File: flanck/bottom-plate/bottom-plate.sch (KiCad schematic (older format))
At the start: 55 parts, among them SW1 SW_PUSH, SW10 SW_PUSH, SW11 SW_PUSH, SW12 SW_PUSH, SW13 SW_PUSH, SW14 SW_PUSH, SW15 SW_PUSH, SW16 SW_PUSH, SW17 SW_PUSH, SW18 SW_PUSH, SW19 SW_PUSH, SW2 SW_PUSH, SW20 SW_PUSH, SW21 SW_PUSH, SW22 SW_PUSH, SW23 SW_PUSH, SW24 SW_PUSH, SW25 SW_PUSH, SW26 SW_PUSH, SW27 SW_PUSH, SW28 SW_PUSH, SW29 SW_PUSH, SW3 SW_PUSH, SW30 SW_PUSH, SW31 SW_PUSH, SW32 SW_PUSH, SW33 SW_PUSH, SW34 SW_PUSH, SW35 SW_PUSH, SW36 SW_PUSH, SW37 SW_PUSH, SW38 SW_PUSH, SW39 SW_PUSH, SW4 SW_PUSH, SW40 SW_PUSH, SW41 SW_PUSH, SW42 SW_PUSH, SW43 SW_PUSH, SW44 SW_PUSH, SW45 SW_PUSH, SW46 SW_PUSH, SW47 SW_PUSH, SW48 SW_PUSH, SW5 SW_PUSH, SW6 SW_PUSH, SW7 SW_PUSH, SW8 SW_PUSH, SW9 SW_PUSH

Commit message: bottom plate
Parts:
- removed SW1, SW10, SW11, SW12, SW13, SW14, SW15, SW16, SW17, SW18, SW19, SW2, SW20, SW21, SW22, SW23, SW24, SW25, SW26, SW27, SW28, SW29, SW3, SW30, SW31, SW32, SW33, SW34, SW35, SW36, SW37, SW38, SW39, SW4, SW40, SW41, SW42, SW43, SW44, SW45, SW46, SW47, SW48, SW5, SW6, SW7, SW8, SW9: SW_PUSH, kbd:SW_Hole, symbol kbd:SW_PUSH

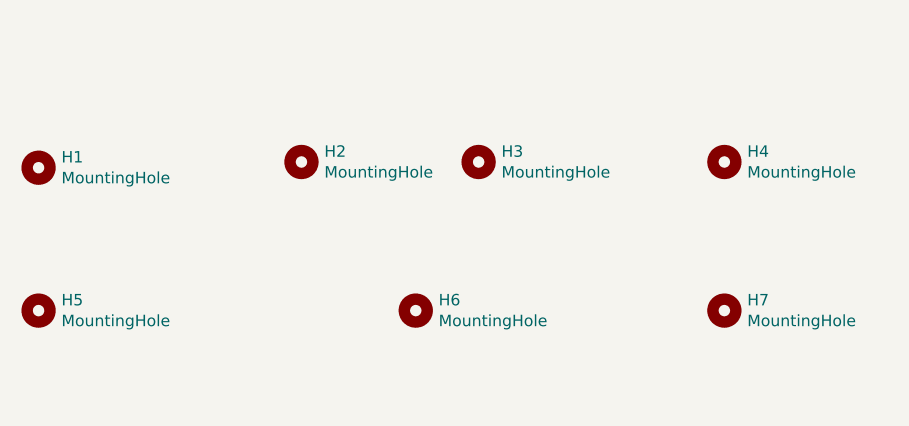
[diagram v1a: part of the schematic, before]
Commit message: fix pcb mounting hole sizes
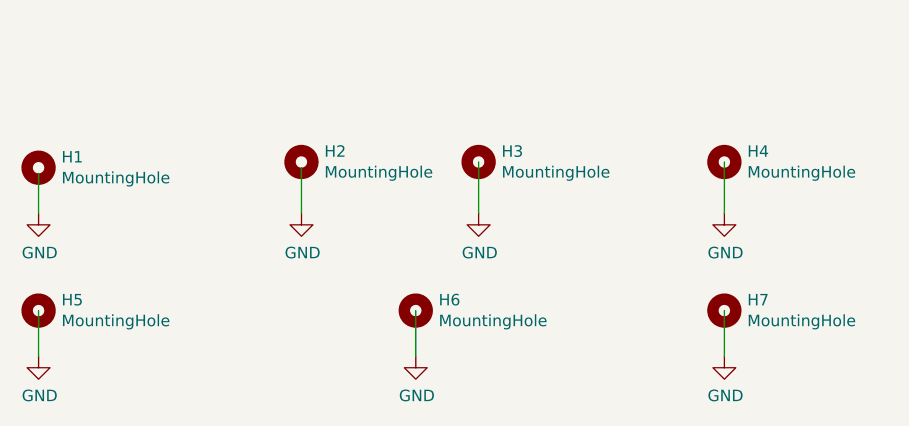
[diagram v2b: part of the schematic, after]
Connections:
- wire segments 0 -> 7
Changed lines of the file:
@@
 	1    0    0    -1
 $EndComp
+$Comp
+L power:GND #PWR?
+U 1 1 5F8D196C
+P 1200 1525
+F 0 "#PWR?" H 1200 1275 50  0001 C CNN
+F 1 "GND" H 1205 1352 50  0000 C CNN
+F 2 "" H 1200 1525 50  0001 C CNN
+F 3 "" H 1200 1525 50  0001 C CNN
+	1    1200 1525
+	1    0    0    -1
+$EndComp
+$Comp
+L power:GND #PWR?
+U 1 1 5F8D1EF3
+P 2350 1525
+F 0 "#PWR?" H 2350 1275 50  0001 C CNN
+F 1 "GND" H 2355 1352 50  0000 C CNN
+F 2 "" H 2350 1525 50  0001 C CNN
+F 3 "" H 2350 1525 50  0001 C CNN
+	1    2350 1525
+	1    0    0    -1
+$EndComp
+$Comp
+L power:GND #PWR?
+U 1 1 5F8D23F4
+P 3125 1525
+F 0 "#PWR?" H 3125 1275 50  0001 C CNN
+F 1 "GND" H 3130 1352 50  0000 C CNN
+F 2 "" H 3125 1525 50  0001 C CNN
+F 3 "" H 3125 1525 50  0001 C CNN
+	1    3125 1525
+	1    0    0    -1
+$EndComp
+$Comp
+L power:GND #PWR?
+U 1 1 5F8D27D4
+P 4200 1525
+F 0 "#PWR?" H 4200 1275 50  0001 C CNN
+F 1 "GND" H 4205 1352 50  0000 C CNN
+F 2 "" H 4200 1525 50  0001 C CNN
+F 3 "" H 4200 1525 50  0001 C CNN
+	1    4200 1525
+	1    0    0    -1
+$EndComp
+$Comp
+L power:GND #PWR?
+U 1 1 5F8D2B0A
+P 1200 2150
+F 0 "#PWR?" H 1200 1900 50  0001 C CNN
+F 1 "GND" H 1205 1977 50  0000 C CNN
+F 2 "" H 1200 2150 50  0001 C CNN
+F 3 "" H 1200 2150 50  0001 C CNN
+	1    1200 2150
+	1    0    0    -1
+$EndComp
+$Comp
+L power:GND #PWR?
+U 1 1 5F8D345C
+P 2850 2150
+F 0 "#PWR?" H 2850 1900 50  0001 C CNN
+F 1 "GND" H 2855 1977 50  0000 C CNN
+F 2 "" H 2850 2150 50  0001 C CNN
+F 3 "" H 2850 2150 50  0001 C CNN
+	1    2850 2150
+	1    0    0    -1
+$EndComp
+$Comp
+L power:GND #PWR?
+U 1 1 5F8D3990
+P 4200 2150
+F 0 "#PWR?" H 4200 1900 50  0001 C CNN
+F 1 "GND" H 4205 1977 50  0000 C CNN
+F 2 "" H 4200 2150 50  0001 C CNN
+F 3 "" H 4200 2150 50  0001 C CNN
+	1    4200 2150
+	1    0    0    -1
+$EndComp
+Wire Wire Line
+	1200 1350 1200 1525
+Wire Wire Line
+	2350 1325 2350 1525
+Wire Wire Line
+	3125 1300 3125 1525
+Wire Wire Line
+	4200 1300 4200 1525
+Wire Wire Line
+	1200 1950 1200 2150
+Wire Wire Line
+	2850 1950 2850 2150
+Wire Wire Line
+	4200 1950 4200 2150
 $EndSCHEMATC
